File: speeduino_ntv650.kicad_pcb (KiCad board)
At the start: 2 copper layers, 75 x 120 mm, 76 parts, among them IC1 SP721, IC2 TC4424, J1 DB25_Male_MountingHoles, J2 Conn_01x01, J3 Conn_01x01, J4 Conn_01x01, J5 Conn_01x01, P1 MAX9926_9927, Q1 STP62NS04Z, Q2 STP62NS04Z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

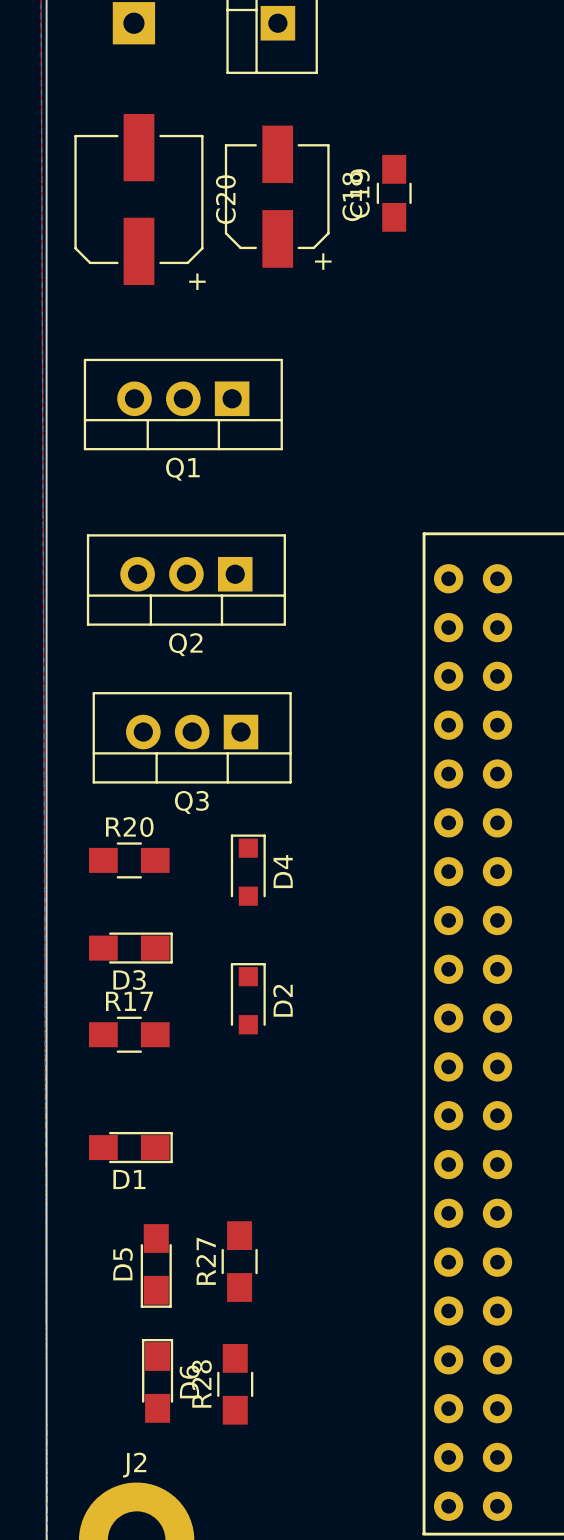
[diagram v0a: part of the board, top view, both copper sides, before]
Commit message: changed its sens schema
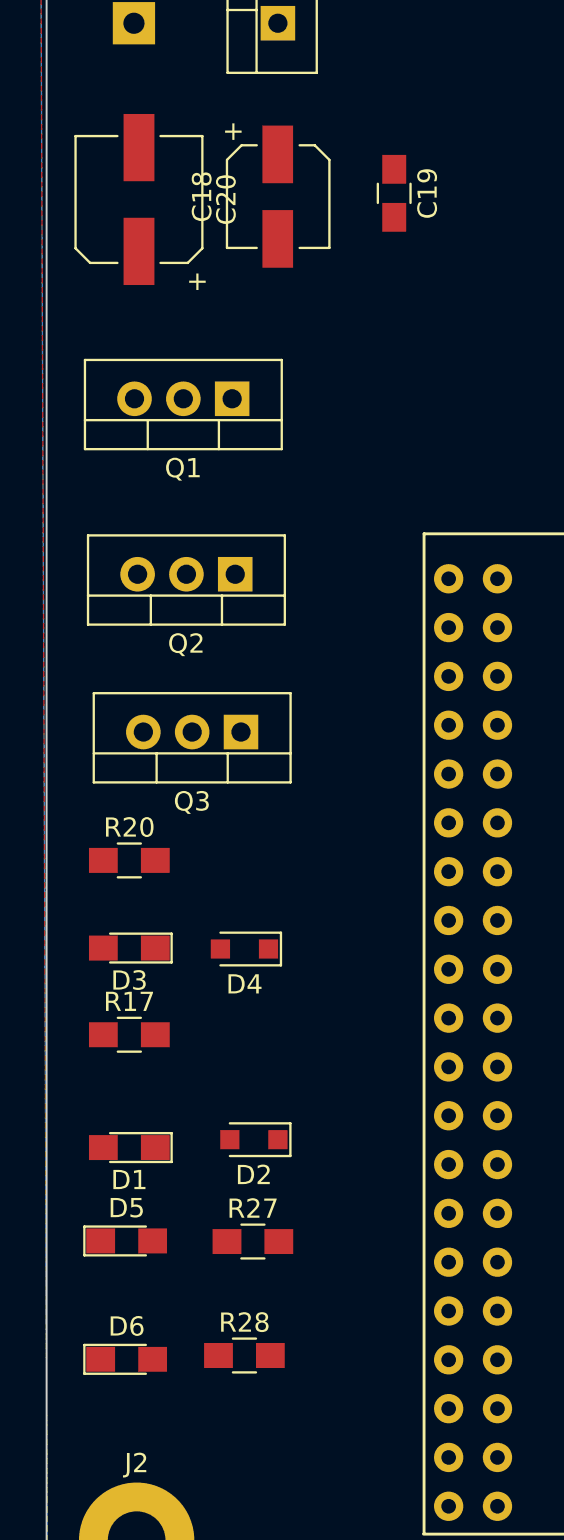
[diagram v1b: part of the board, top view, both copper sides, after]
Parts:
- moved D2 7.24 mm to (60.6, 145.3), turned to 180 degrees
- moved D4 4.00 mm to (60.1, 135.4), turned to 180 degrees
- moved D6 2.01 mm to (54.0, 156.7), turned to 0 degrees
- moved D5 1.96 mm to (54.0, 150.6), turned to 0 degrees
- moved R28 1.57 mm to (60.1, 156.5), turned to 0 degrees
- moved R27 1.25 mm to (60.6, 150.6), turned to 0 degrees
- turned C18 to 270 degrees
- turned C19 to 270 degrees
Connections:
- J1 pad 4: (no net) -> 5V

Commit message: pcb frame complited
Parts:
- added J6: Conn_01x01, Mounting_Holes:MountingHole_3mm_Pad_Via, F.Cu at (119.1, 100.5)
- added J7: Conn_01x01, Mounting_Holes:MountingHole_3mm_Pad_Via, F.Cu at (179.1, 100.5)
- J1: value DB25_Male_MountingHoles -> DB25_Female_MountingHoles; footprint Connector_Dsub:DSUB-25_Male_Horizontal_P2.77x2.84mm_EdgePinOffset4.94mm_Housed_MountingHolesOffset7.48mm -> ntv650_ecu:DSUB-25_Female_Horizontal_P2.77x2.84mm_EdgePinOffset4.94mm_Housed_MountingHolesOffset7.48mm
- J2, J3, J4, J5: footprint MountingHole:MountingHole_3mm_Pad -> Mounting_Holes:MountingHole_3mm_Pad_Via
- RV1: footprint Varistors:RV_Disc_D15.5_W3.9_P7.5 -> Varistors:RV_Disc_D9_W3.3_P5
- moved Q3 83.2 mm to (134.8, 87.7), turned to 270 degrees
- moved C5 77.5 mm to (157.2, 143.7)
- moved R2 77.5 mm to (157.2, 140.0)
- moved D7 75.9 mm to (127.2, 65.8), turned to 270 degrees
- moved C15 74.4 mm to (182.1, 72.1)
- moved R26 74.4 mm to (177.1, 71.8)
- moved Q2 72.5 mm to (126.6, 88.0), turned to 270 degrees
- moved U1 72.4 mm to (126.7, 55.2), turned to 270 degrees
- moved D5 71.4 mm to (123.2, 132.8), turned to 180 degrees
- moved J2 69.6 mm to (119.1, 140.0)
- moved RV1 69.2 mm to (120.4, 54.8), turned to 180 degrees
- moved D2 66.7 mm to (122.9, 121.5)
- moved D3 66.7 mm to (116.5, 111.5)
- moved D4 66.7 mm to (122.4, 111.5)
- moved D6 66.7 mm to (116.3, 132.9)
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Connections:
- J1 pad 1: VR1+ -> GND
- J1 pad 10: ign-1-out -> 5V
- J1 pad 11: idle-out -> MAP
- J1 pad 12: 12V -> VR2+
- J1 pad 13: GND -> VR1+
- J1 pad 14: VR1- -> GND
- J1 pad 15: VR2- -> 12V
- J1 pad 16: GND -> ign-2-out
- J1 pad 17: GND -> inj-2-out
- J1 pad 18: TPS_sens -> STEP-2B-OUT
- J1 pad 19: ITS_sens -> STEP-1B-OUT
- J1 pad 2: VR2+ -> 12V
- J1 pad 20: STEP-1B-OUT -> ITS_sens
- J1 pad 21: STEP-2B-OUT -> TPS_sens
- J1 pad 22: inj-2-out -> GND
- J1 pad 23: ign-2-out -> GND
- J1 pad 24: 12V -> VR2-
- J1 pad 25: GND -> VR1-
- J1 pad 3: MAP -> idle-out
- J1 pad 4: 5V -> ign-1-out
- J1 pad 5: O2_sens -> inj-1-out
- J1 pad 6: CLT_sens -> STEP-2A-OUT
- J1 pad 8: STEP-2A-OUT -> CLT_sens
- J1 pad 9: inj-1-out -> O2_sens
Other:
- board size 75 x 120 mm -> 74 x 119 mm

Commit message: pcb change some positions
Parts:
- moved R26 30.5 mm to (154.9, 92.8)
- moved C15 30.1 mm to (160.2, 92.7)
- moved C9 12.2 mm to (181.4, 92.7)
- moved C4 12.2 mm to (176.1, 92.7)
- moved C1 11.7 mm to (165.5, 92.7)
- moved R25 11.4 mm to (170.8, 92.8)
- moved R17 11.0 mm to (122.7, 107.0)
- moved R24 6.34 mm to (171.4, 140.2)
- moved P1 5.41 mm to (173.8, 74.2)
- moved C12 4.56 mm to (176.1, 86.6)
- moved C11 4.53 mm to (147.5, 62.9)
- moved R29 4.37 mm to (141.8, 56.1)
- moved R30 4.37 mm to (137.2, 56.0)
- moved R23 4.31 mm to (171.4, 148.9)
- moved R11 4.02 mm to (181.4, 86.7)
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
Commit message: pcb change some positions again
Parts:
- moved C19 2.50 mm to (130.8, 77.1)
- moved C18 2.12 mm to (125.3, 78.8)
- moved U1 1.35 mm to (127.0, 54.8)
- moved D7 1.06 mm to (127.8, 65.9)
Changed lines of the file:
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@@
   )
   (module Capacitors_SMD:C_0805_HandSoldering placed (layer F.Cu)
-    (at 133.14 77.86 270)
+    (at 130.77 77.06 270)
     (descr "Capacitor SMD 0805, hand soldering")
     (tags "capacitor 0805")
@@
   )
   (module Diodes_ThroughHole:D_DO-41_SOD81_P5.08mm_Vertical_KathodeUp placed (layer F.Cu)
-    (at 128.81 65.64 270)
+    (at 127.77 65.86 270)
     (descr "D, DO-41_SOD81 series, Axial, Vertical, pin pitch=5.08mm, , length*diameter=5.2*2.7mm^2, , http://www.diodes.com/_files/packages/DO-41%20(Plastic).pdf")
     (tags "D DO-41_SOD81 series Axial Vertical pin pitch 5.08mm  length 5.2mm diameter 2.7mm")
@@
   )
   (module Capacitors_SMD:CP_Elec_5x5.3 placed (layer F.Cu)
-    (at 127.13 77.7 270)
+    (at 125.31 78.79 270)
     (descr "SMT capacitor, aluminium electrolytic, 5x5.3")
     (attr smd)
@@
   )
   (module TO_SOT_Packages_THT:TO-220-3_Vertical placed (layer F.Cu)
-    (at 128.38 54.99 270)
+    (at 127.04 54.84 270)
     (descr "TO-220-3, Vertical, RM 2.54mm")
     (tags "TO-220-3 Vertical RM 2.54mm")

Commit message: routing complite
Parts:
- C11, C21, C3, R10, R3, R4, R5, R6, R7: moved to B.Cu
- J2, J3, J4, J5, J6, J7: footprint Mounting_Holes:MountingHole_3mm_Pad_Via -> Mounting_Holes:MountingHole_3mm_Pad
- moved R29 22.8 mm to (147.0, 78.4)
- moved R30 22.8 mm to (142.4, 78.2)
- moved A1 9.64 mm to (150.5, 81.4)
- moved D6 9.14 mm to (122.8, 126.4), turned to 180 degrees
- moved R27 9.08 mm to (116.3, 132.9), turned to 180 degrees
- moved P1 5.28 mm to (179.0, 74.4)
- moved C11 3.72 mm to (151.1, 62.0)
- moved R10 3.65 mm to (152.6, 57.2)
- moved R7 2.92 mm to (156.7, 57.2)
- moved R5 2.19 mm to (160.7, 57.2)
- moved D7 1.92 mm to (129.7, 65.9)
- moved U1 1.92 mm to (129.0, 54.8)
- moved R26 1.67 mm to (156.6, 92.8)
- moved R15 1.51 mm to (156.4, 86.8)
- moved R6 1.46 mm to (164.8, 57.2)
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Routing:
- net GND: track 0.00 -> 623.9 mm, vias 0 -> 6
- net 5V: track 0.00 -> 248.1 mm, vias 0 -> 2
- net ADC-Clamp5: track 0.00 -> 179.8 mm
- net 12V: track 0.00 -> 175.2 mm, vias 0 -> 2
- net TACH2-CPU-D18: track 0.00 -> 161.2 mm, vias 0 -> 2
- net ign-2-out: track 0.00 -> 144.9 mm, vias 0 -> 1
- net O2_sens: track 0.00 -> 144.2 mm, vias 0 -> 2
- net inj-1-out: track 0.00 -> 117.5 mm, vias 0 -> 1
- net Net-(IC2-Pad2): track 0.00 -> 113.8 mm, vias 0 -> 1
- net ign-1-out: track 0.00 -> 95.6 mm, vias 0 -> 1
- net CLT_sens: track 0.00 -> 94.3 mm
- net STEPEN-CPU-D24: track 0.00 -> 91.6 mm
- net TPS_sens: track 0.00 -> 88.9 mm
- net inj-2-out: track 0.00 -> 87.0 mm
- net Net-(IC2-Pad4): track 0.00 -> 84.5 mm, vias 0 -> 1
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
